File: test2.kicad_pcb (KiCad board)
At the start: 2 copper layers, 80 x 40 mm, 24 parts, among them IC1 2EDN8534FXTMA1, J10 Master, J6 XT 60, J8 XT 60, J9 FCCU, Q1 IRFP4468PBF, Q2 IRLIZ44N, Q3 IRLIZ44N, Q4 IRFP4468PBF, U1 HO 25-P

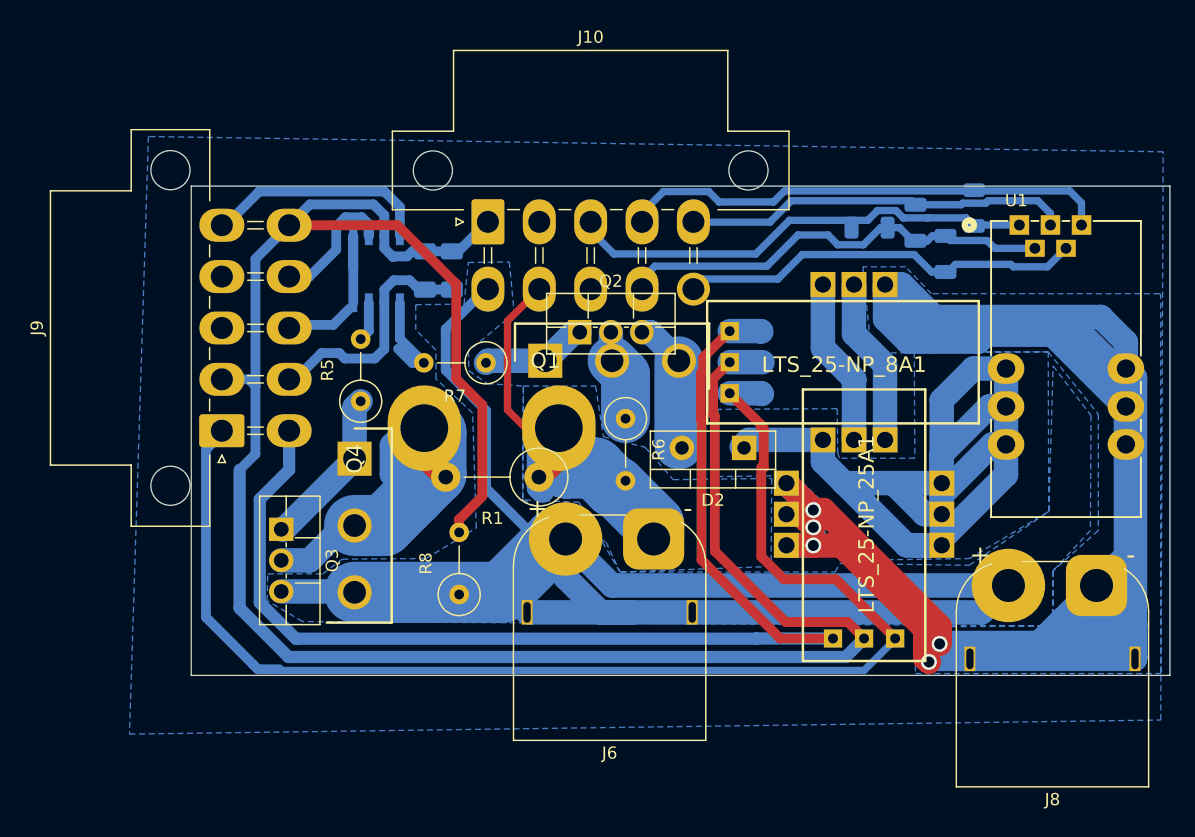
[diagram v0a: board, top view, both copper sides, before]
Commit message: Add 3d models
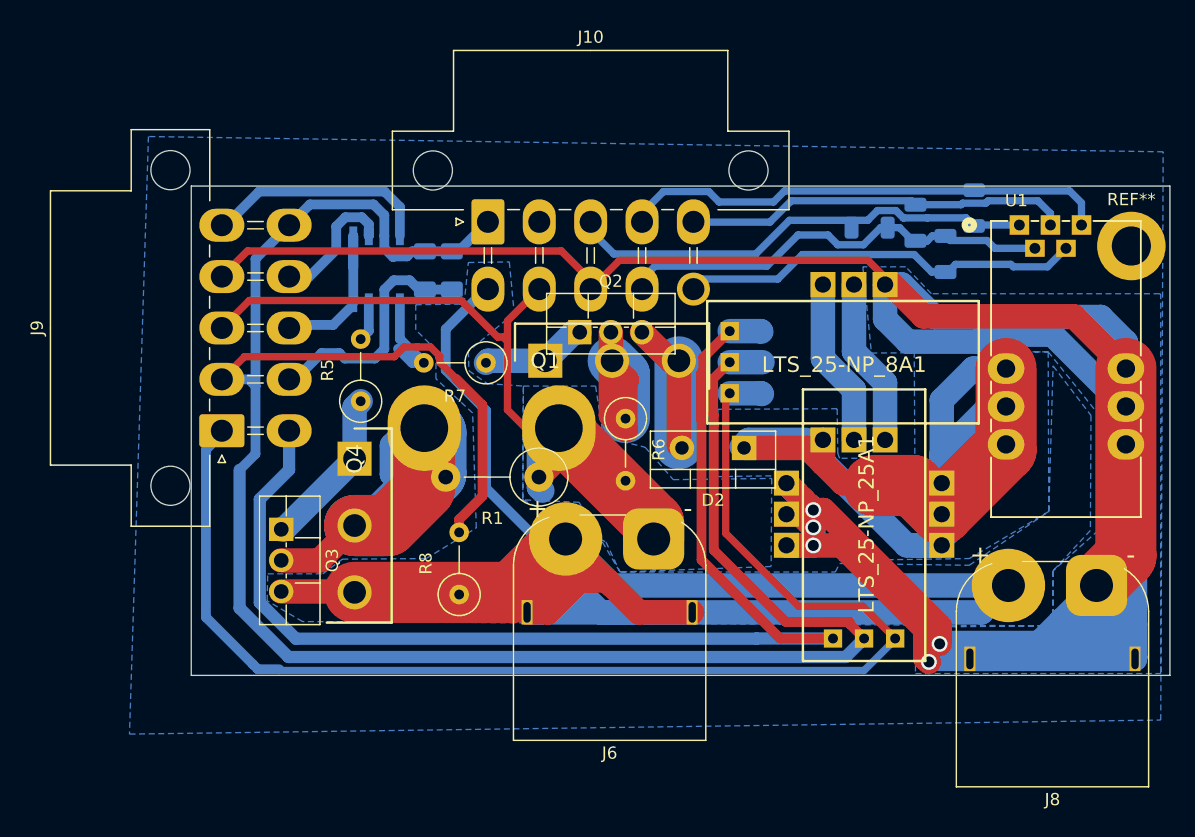
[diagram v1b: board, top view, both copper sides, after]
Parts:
- added REF**: MountingHole_3.2mm_M3_DIN965_Pad, MountingHole:MountingHole_3.2mm_M3_DIN965_Pad, F.Cu at (234.4, 41.9)
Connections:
- J10 pad 10: /0V -> /Vref
- J10 pad 4: /Out -> /OCD
- J10 pad 5: /OCD -> /Out
- J10 pad 7: /XT 60 Super Capacitors -> /XT60 Fuel Cell
- J10 pad 8: /XT60 Fuel Cell -> /XT 60 Super Capacitors
- J10 pad 9: /Vref -> /0V
- J9 pad 3: /XT 60 Super Capacitors -> /XT60 Fuel Cell
- J9 pad 4: /XT60 Fuel Cell -> /XT 60 Super Capacitors
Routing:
- net /XT 60 Super Capacitors: track 225.6 -> 311.0 mm
- net /Hall_in: track 87.9 -> 139.4 mm
- net /XT60 Fuel Cell: track 43.4 -> 65.8 mm
- net Earth: track 139.7 -> 160.5 mm
- net Net-(Q1-D): track 7.56 -> 19.9 mm
- net Net-(Q3-D): track 33.2 -> 45.2 mm
- net Net-(D2-A): track 11.2 -> 18.4 mm
- net GND: track 183.2 -> 181.5 mm
